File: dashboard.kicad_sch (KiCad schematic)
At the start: 30 parts, among them J1 DT13-12PA-B016, J3 RJ45, J5 776267-1, Q1 2N7002, SW1 SW_Push, SW2 SW_SPST, SW4 SW_SPST, U1 TPS542025DDC, U4 ILD74

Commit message: Route PCB
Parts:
- removed J1: DT13-12PA-B016, symbol Connector_Generic:Conn_01x12
- added C8, C9: 10u, Capacitor_THT:C_Disc_D5.1mm_W3.2mm_P5.00mm, symbol Device:C_Small
- added J2: Conn_01x02, Connector_JST:JST_EH_B2B-EH-A_1x02_P2.50mm_Vertical, symbol Connector_Generic:Conn_01x02
- added J4: Conn_01x10, Connector_JST:JST_EH_B10B-EH-A_1x10_P2.50mm_Vertical, symbol Connector_Generic:Conn_01x10
- added L3: 12u, Inductor_SMD:L_Wuerth_WE-PD-Typ-7345, symbol Device:L_Small
- added U2: R-78C5.0-1.0, Converter_DCDC:Converter_DCDC_RECOM_R-78E-0.5_THT, symbol Regulator_Switching:R-78C5.0-1.0
- C1, C2, C3, C4: footprint (none) -> Capacitor_SMD:C_0805_2012Metric_Pad1.18x1.45mm_HandSolder; now left out of the parts list
- C5, C7: footprint (none) -> Capacitor_SMD:C_1210_3225Metric_Pad1.33x2.70mm_HandSolder; now left out of the parts list
- C6: footprint (none) -> Capacitor_SMD:C_Elec_6.3x5.8; now left out of the parts list
- D2, ESTOP1, SW4, U1: now left out of the parts list
- L1: footprint (none) -> Inductor_SMD:L_TDK_SLF12575; now left out of the parts list
- L2: value 470n -> 560n; footprint (none) -> Inductor_SMD:L_Wuerth_MAPI-3012; now left out of the parts list
- Q1: footprint Package_TO_SOT_SMD:SOT-23 -> Package_TO_SOT_THT:TO-92L_Inline_Wide
- R1: footprint (none) -> Resistor_THT:R_Axial_DIN0207_L6.3mm_D2.5mm_P7.62mm_Horizontal
- R2: footprint (none) -> Resistor_SMD:R_0805_2012Metric_Pad1.20x1.40mm_HandSolder; now left out of the parts list
- R6, R7: footprint Resistor_SMD:R_0603_1608Metric_Pad0.98x0.95mm_HandSolder -> Resistor_THT:R_Axial_DIN0207_L6.3mm_D2.5mm_P7.62mm_Horizontal
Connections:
- net +12V: now also C8.1, J4.5 (Pin_5), L3.1
- net +5V: now also J4.3 (Pin_3), U2.3 (OUT)
- net Fan_Sig: now also J4.7 (Pin_7)
- net GND: now also C8.2, C9.2, J4.10 (Pin_10), J4.4 (Pin_4), J4.8 (Pin_8), U2.2 (GND)
- net Neutral: now also J4.2 (Pin_2)
- net Neutral_LED+: now also J4.1 (Pin_1)
- net Shutdown1: now also J2.1 (Pin_1)
- net Shutdown2: now also J2.2 (Pin_2)
- net Spare_Switch_Sig: now also J4.9 (Pin_9)
- net Starter_Sig: now also J4.6 (Pin_6)
- new net: C9.1, L3.2, U2.1 (IN)
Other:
- note added: "Dashboard Left"
- note added: "Dashbord Right"
- note added: "Designed using TE Power Supply Designer https://webench.ti.com/appinfo/webench/scripts/SDP.cgi?ID=440B08FC1444BCED"
- note added: "ONLY POPULATE ONE"
- note added: "Power Supply (A)"
- note added: "Power Supply (B)"
- note added: "WARNING!"
- note removed: "Designed using TE Power Supply Designer https://webench.ti.com/power-designer/switching-regulator"
- note removed: "LED Power Control"
- moved on the sheet: C1, C2, C3, C4, C5, C6, C7, D1, D2, ESTOP1, H1, H2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

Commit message: Add both power supplies
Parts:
- C1, C2, C3, C4, C5, C6, C7, L1, L2, R2, U1: now in the parts list
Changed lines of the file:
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@@
 		(unit 1)
 		(exclude_from_sim no)
-		(in_bom no)
-		(on_board no)
+		(in_bom yes)
+		(on_board yes)
 		(dnp no)
 		(fields_autoplaced yes)
@@
 		(unit 1)
 		(exclude_from_sim no)
-		(in_bom no)
-		(on_board no)
+		(in_bom yes)
+		(on_board yes)
 		(dnp no)
 		(fields_autoplaced yes)
@@
 		(unit 1)
 		(exclude_from_sim no)
-		(in_bom no)
-		(on_board no)
+		(in_bom yes)
+		(on_board yes)
 		(dnp no)
 		(fields_autoplaced yes)
@@
 		(unit 1)
 		(exclude_from_sim no)
-		(in_bom no)
-		(on_board no)
+		(in_bom yes)
+		(on_board yes)
 		(dnp no)
 		(fields_autoplaced yes)
@@
 		(unit 1)
 		(exclude_from_sim no)
-		(in_bom no)
-		(on_board no)
+		(in_bom yes)
+		(on_board yes)
 		(dnp no)
 		(property "Reference" "C2"
@@
 		(unit 1)
 		(exclude_from_sim no)
-		(in_bom no)
-		(on_board no)
+		(in_bom yes)
+		(on_board yes)
 		(dnp no)
 		(property "Reference" "C1"
@@
 		(unit 1)
 		(exclude_from_sim no)
-		(in_bom no)
-		(on_board no)
+		(in_bom yes)
+		(on_board yes)
 		(dnp no)
 		(fields_autoplaced yes)
@@
 		(unit 1)
 		(exclude_from_sim no)
-		(in_bom no)
-		(on_board no)
+		(in_bom yes)
+		(on_board yes)
 		(dnp no)
 		(property "Reference" "#PWR014"
@@
 		(unit 1)
 		(exclude_from_sim no)
-		(in_bom no)
-		(on_board no)
+		(in_bom yes)
+		(on_board yes)
 		(dnp no)
 		(fields_autoplaced yes)
@@
 		(unit 1)
 		(exclude_from_sim no)
-		(in_bom no)
-		(on_board no)
+		(in_bom yes)
+		(on_board yes)
 		(dnp no)
 		(fields_autoplaced yes)
@@
 		(unit 1)
 		(exclude_from_sim no)
-		(in_bom no)
-		(on_board no)
+		(in_bom yes)
+		(on_board yes)
 		(dnp no)
 		(fields_autoplaced yes)
@@
 		(unit 1)
 		(exclude_from_sim no)
-		(in_bom no)
-		(on_board no)
+		(in_bom yes)
+		(on_board yes)
 		(dnp no)
 		(fields_autoplaced yes)
@@
 		(unit 1)
 		(exclude_from_sim no)
-		(in_bom no)
-		(on_board no)
+		(in_bom yes)
+		(on_board yes)
 		(dnp no)
 		(property "Reference" "L1"
@@
 		(unit 1)
 		(exclude_from_sim no)
-		(in_bom no)
-		(on_board no)
+		(in_bom yes)
+		(on_board yes)
 		(dnp no)
 		(fields_autoplaced yes)
@@
 		(unit 1)
 		(exclude_from_sim no)
-		(in_bom no)
-		(on_board no)
+		(in_bom yes)
+		(on_board yes)
 		(dnp no)
 		(property "Reference" "C3"
@@
 		(unit 1)
 		(exclude_from_sim no)
-		(in_bom no)
-		(on_board no)
+		(in_bom yes)
+		(on_board yes)
 		(dnp no)
 		(fields_autoplaced yes)

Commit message: Add power supply protection
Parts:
- added D3: SS34, Diode_SMD:D_SMA, symbol Diode:SS34
- added D4: SMBJ24CA, Diode_SMD:D_SMB_Handsoldering, symbol Device:D_TVS
- added F2: MF-USHTD75KX/24-2, Fuse:Fuse_1210_3225Metric_Pad1.42x2.65mm_HandSolder, symbol Device:Polyfuse
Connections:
- net +12V: now also F2.1; no longer C7.1, C8.1, L2.1, L3.1
- net GND: now also D4.1 (A1)
- new net: D3.1 (K), F2.2
- new net PSU+: C7.1, C8.1, D3.2 (A), D4.2 (A2), L2.1, L3.1
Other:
- note added: "ONLY POPULATE ONE OF A/B"
- note added: "Protection"
- note removed: "ONLY POPULATE ONE"
- moved on the sheet: C1, C2, C3, C4, C5, C6, C7, C8, C9, L1, L2, L3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

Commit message: Revert "Add power supply protection"
This reverts commit 6c38df0548b9625adbd3b6c051cb9005b09ba150.
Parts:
- removed D3: SS34, Diode_SMD:D_SMA, symbol Diode:SS34
- removed D4: SMBJ24CA, Diode_SMD:D_SMB_Handsoldering, symbol Device:D_TVS
- removed F2: MF-USHTD75KX/24-2, Fuse:Fuse_1210_3225Metric_Pad1.42x2.65mm_HandSolder, symbol Device:Polyfuse
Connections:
- net PSU+ is gone; now on net +12V: C7.1, C8.1, L2.1, L3.1
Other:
- note added: "ONLY POPULATE ONE"
- note removed: "ONLY POPULATE ONE OF A/B"
- note removed: "Protection"
- moved on the sheet: C1, C2, C3, C4, C5, C6, C7, C8, C9, L1, L2, L3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

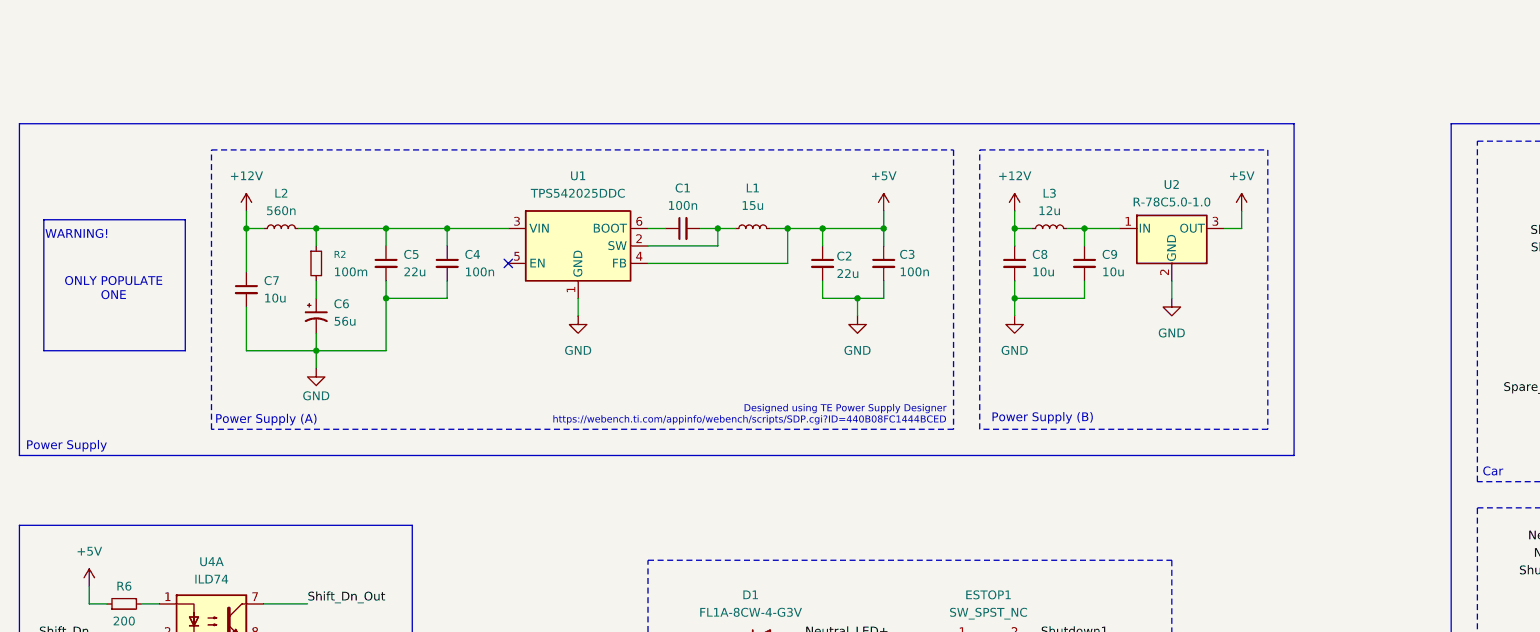
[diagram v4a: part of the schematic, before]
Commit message: added protection for switching regulator, rerouted PCB
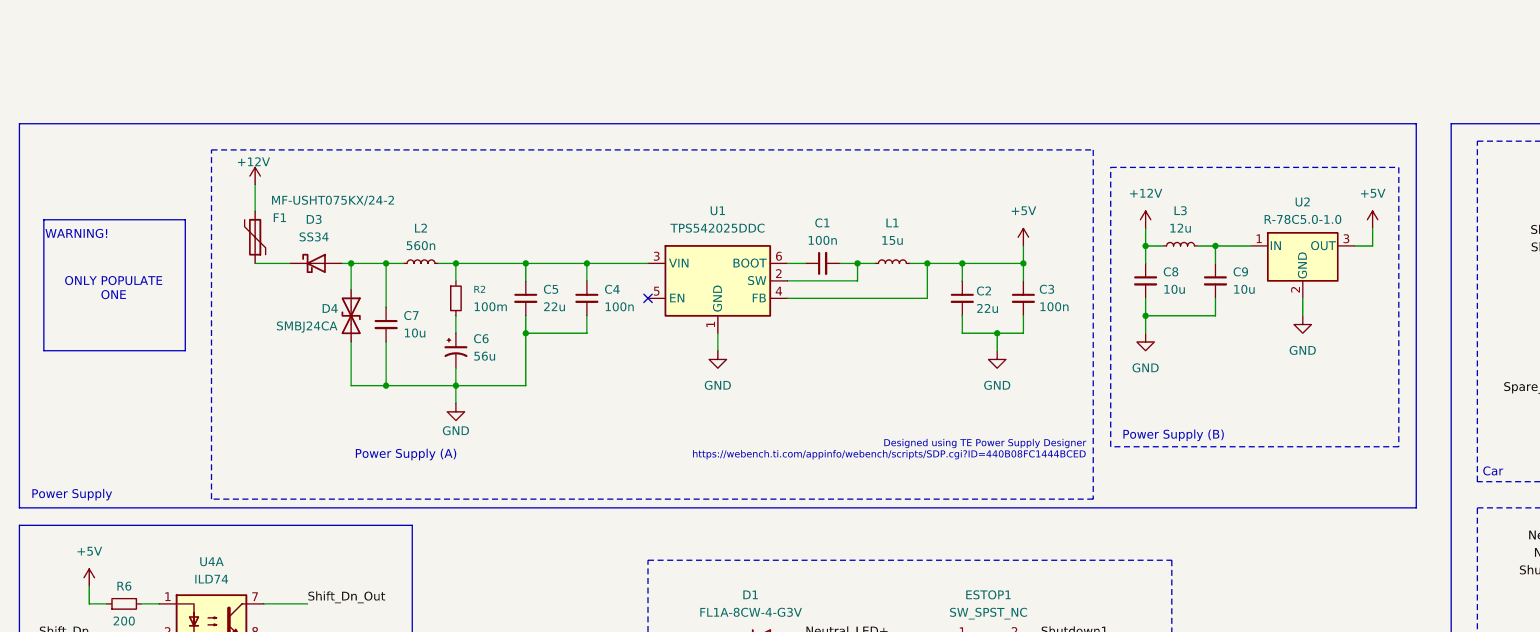
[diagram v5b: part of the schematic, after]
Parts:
- added D3: SS34, Diode_SMD:D_SMA, symbol Diode:SS34
- added D4: SMBJ24CA, Diode_SMD:D_SMB, symbol Device:D_TVS
- added F1: MF-USHT075KX/24-2, Inductor_SMD:L_1210_3225Metric, symbol Device:Polyfuse
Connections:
- net +12V: now also F1.2; no longer C7.1, L2.1
- net GND: now also D4.2 (A2)
- new net: D3.1 (K), F1.1
- new net: C7.1, D3.2 (A), D4.1 (A1), L2.1
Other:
- moved on the sheet: C1, C2, C3, C4, C5, C6, C7, C8, C9, L1, L2, L3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

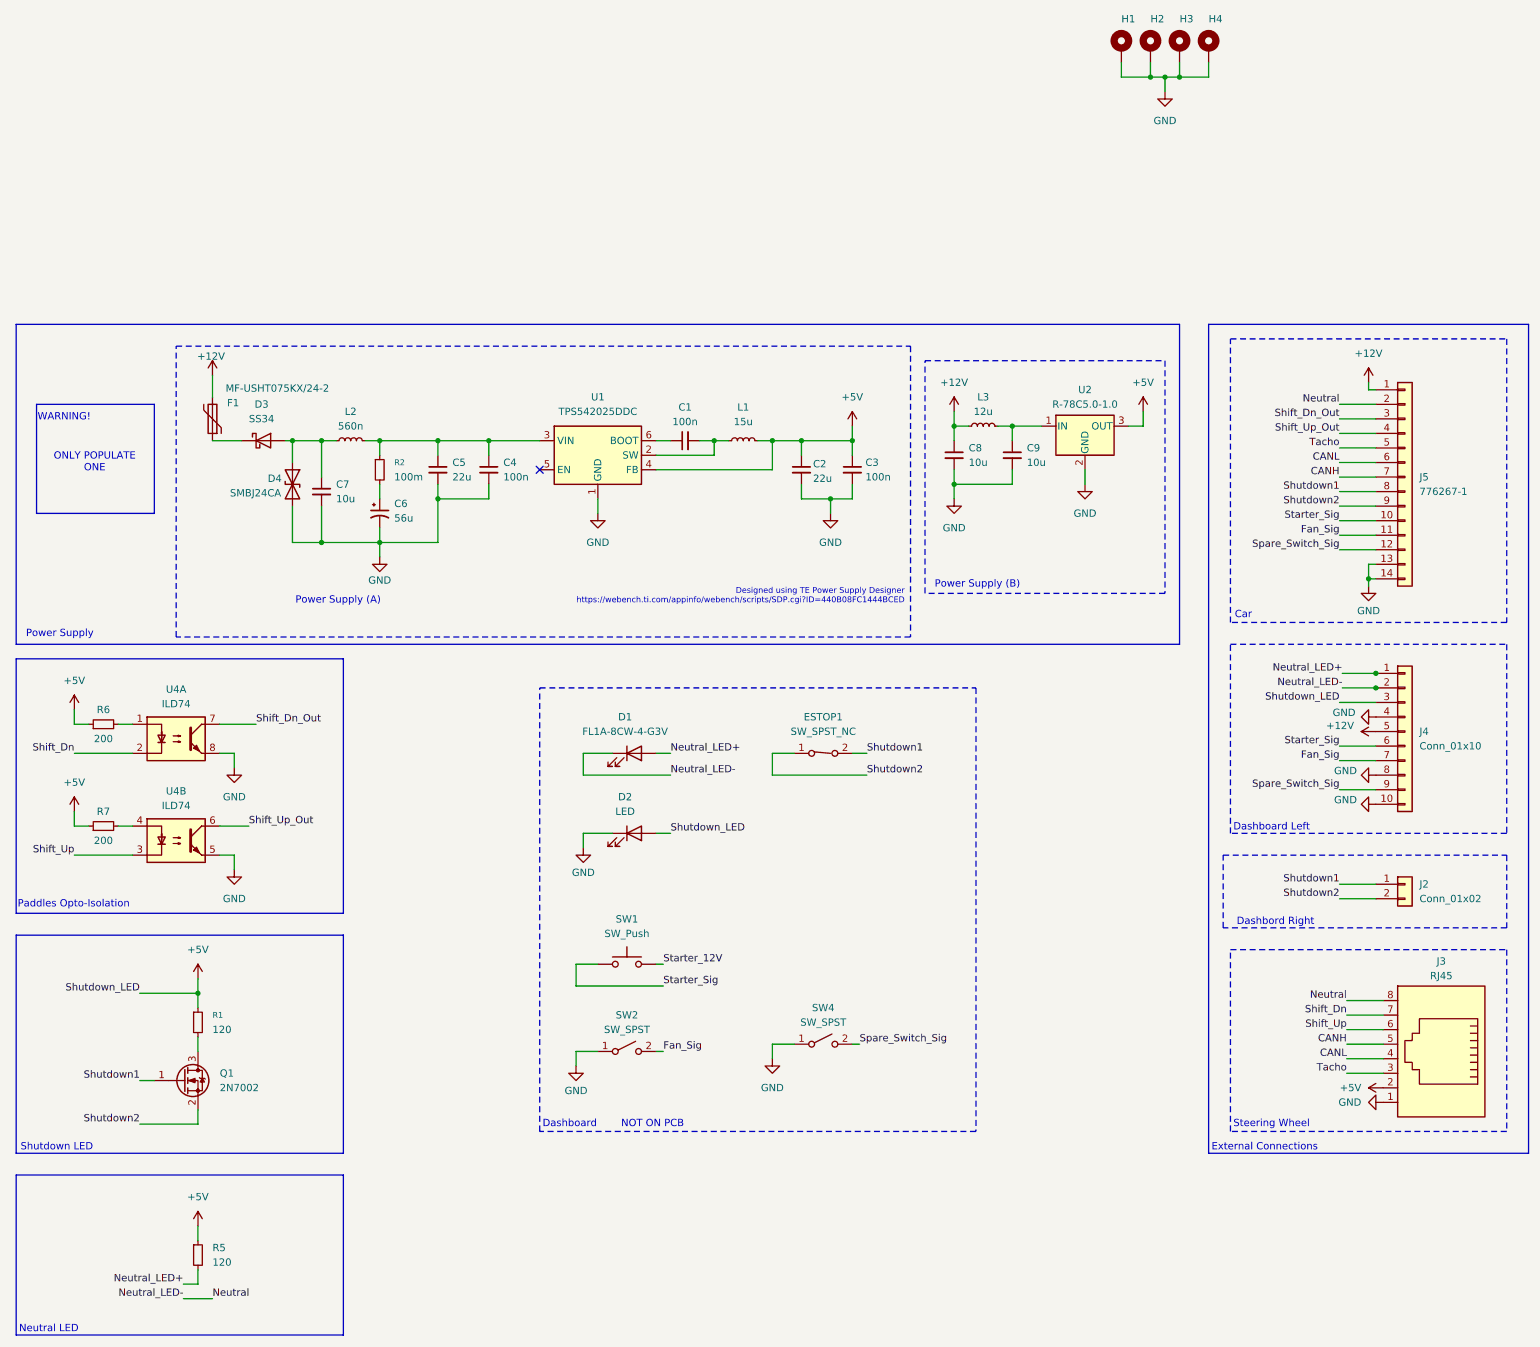
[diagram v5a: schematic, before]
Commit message: Add power supply protection
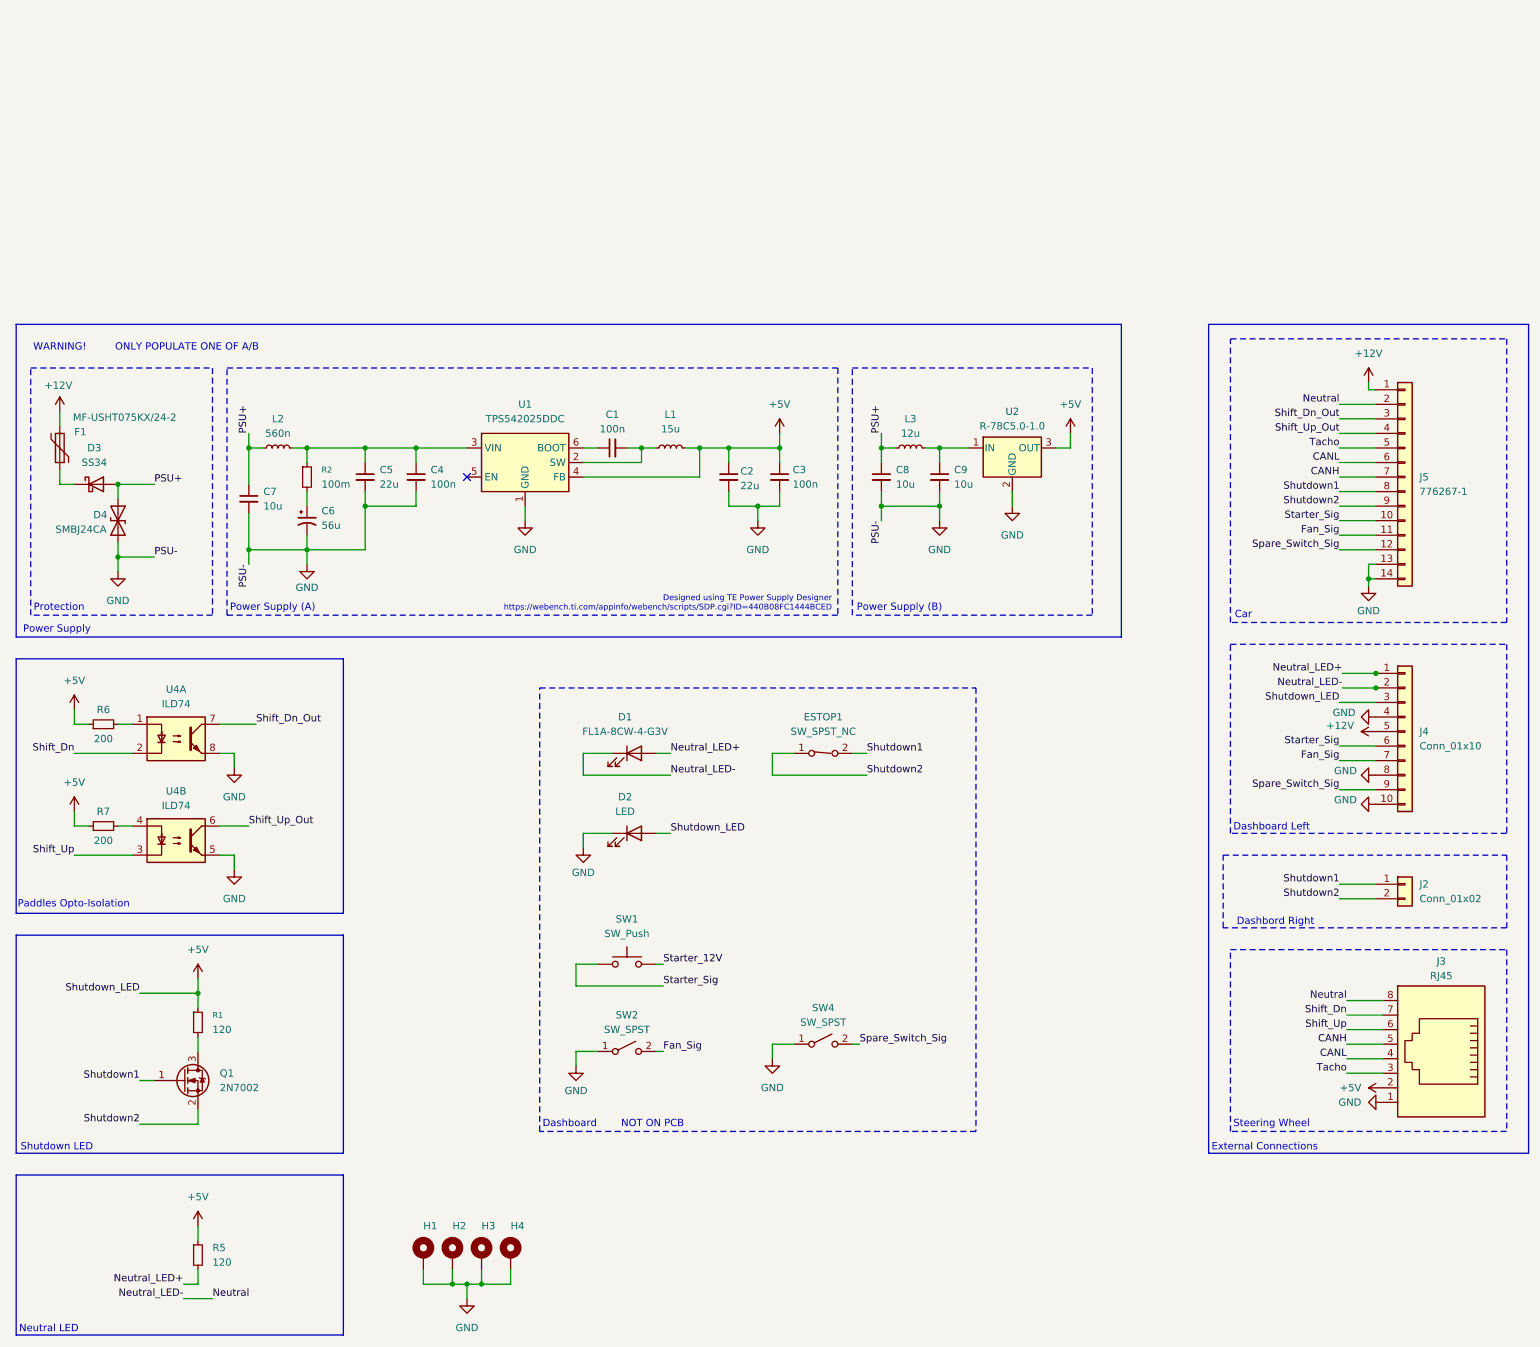
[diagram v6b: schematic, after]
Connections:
- net +12V: no longer C8.1, L3.1
- net PSU+: now reaches C7.1, D3.2 (A), D4.1 (A1), L2.1
- net PSU+: now also C8.1, L3.1
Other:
- note added: "ONLY POPULATE ONE OF A/B"
- note added: "Protection"
- note removed: "ONLY POPULATE ONE"
- moved on the sheet: C1, C2, C3, C4, C5, C6, C7, C8, C9, D3, D4, F1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

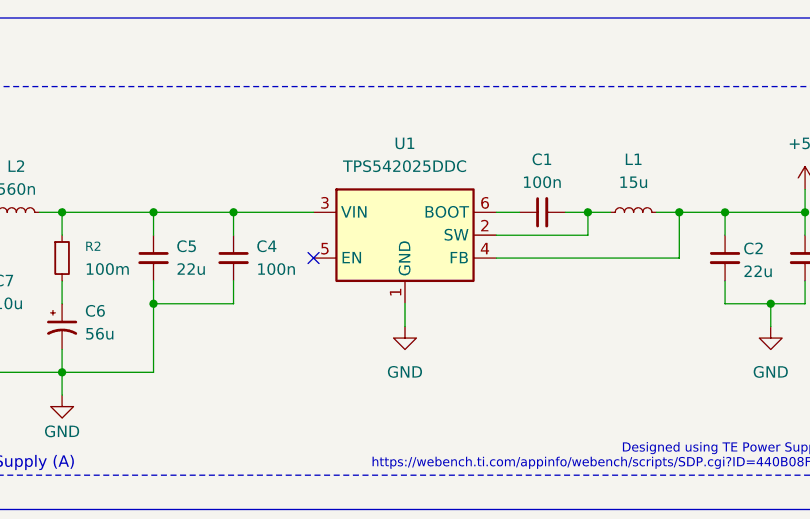
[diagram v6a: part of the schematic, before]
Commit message: added thermal vias for TPS54
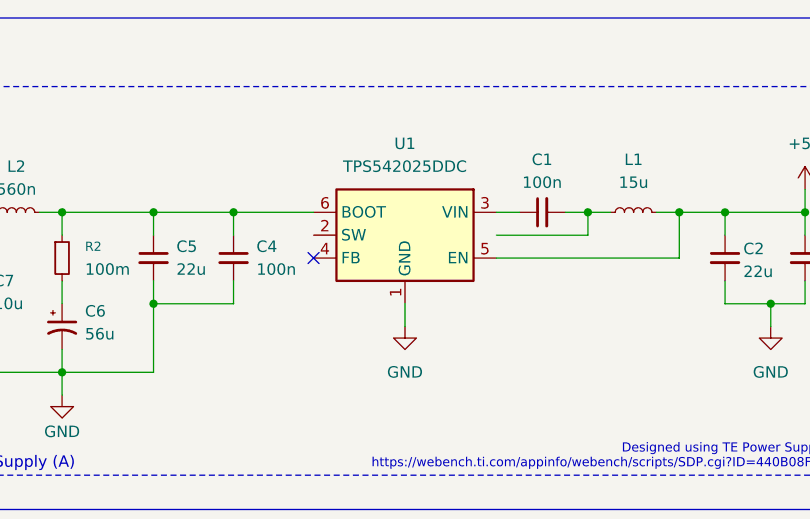
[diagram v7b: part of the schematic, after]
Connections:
- net +5V: now also U1.5 (EN); no longer U1.4 (FB)
- net at C4.1, C5.1, L2.2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: now also U1.6 (BOOT); no longer U1.3 (VIN)
- net at C1.2, L1.1: no longer U1.2 (SW)
- net at C1.1: now also U1.3 (VIN); no longer U1.6 (BOOT)
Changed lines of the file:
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@@
 		(lib_id "Regulator_Switching:TPS54202DDC")
 		(at 105.41 40.64 0)
-		(unit 1)
-		(exclude_from_sim no)
-		(in_bom yes)
-		(on_board yes)
-		(dnp no)
-		(fields_autoplaced yes)
+		(mirror y)
+		(unit 1)
+		(exclude_from_sim no)
+		(in_bom yes)
+		(on_board yes)
+		(dnp no)
 		(property "Reference" "U1"
 			(at 105.41 30.48 0)
@@
 		)
 		(property "Footprint" "Package_TO_SOT_SMD:SOT-23-6"
-			(at 106.68 49.53 0)
+			(at 104.14 49.53 0)
 			(effects
 				(font
@@
 		)
 		(property "Datasheet" "http://www.ti.com/lit/ds/symlink/tps54202.pdf"
-			(at 97.79 31.75 0)
+			(at 113.03 31.75 0)
 			(effects
 				(font
@@
 		)
 		(instances
-			(project ""
+			(project "dashboard"
 				(path "/e03820ab-31df-4dd3-bbbf-004e9f7c6b92"
 					(reference "#PWR024")
